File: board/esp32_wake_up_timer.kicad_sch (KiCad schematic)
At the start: 6 parts, among them SW1 SW_DIP_x01, SW3 Rotary Encoder

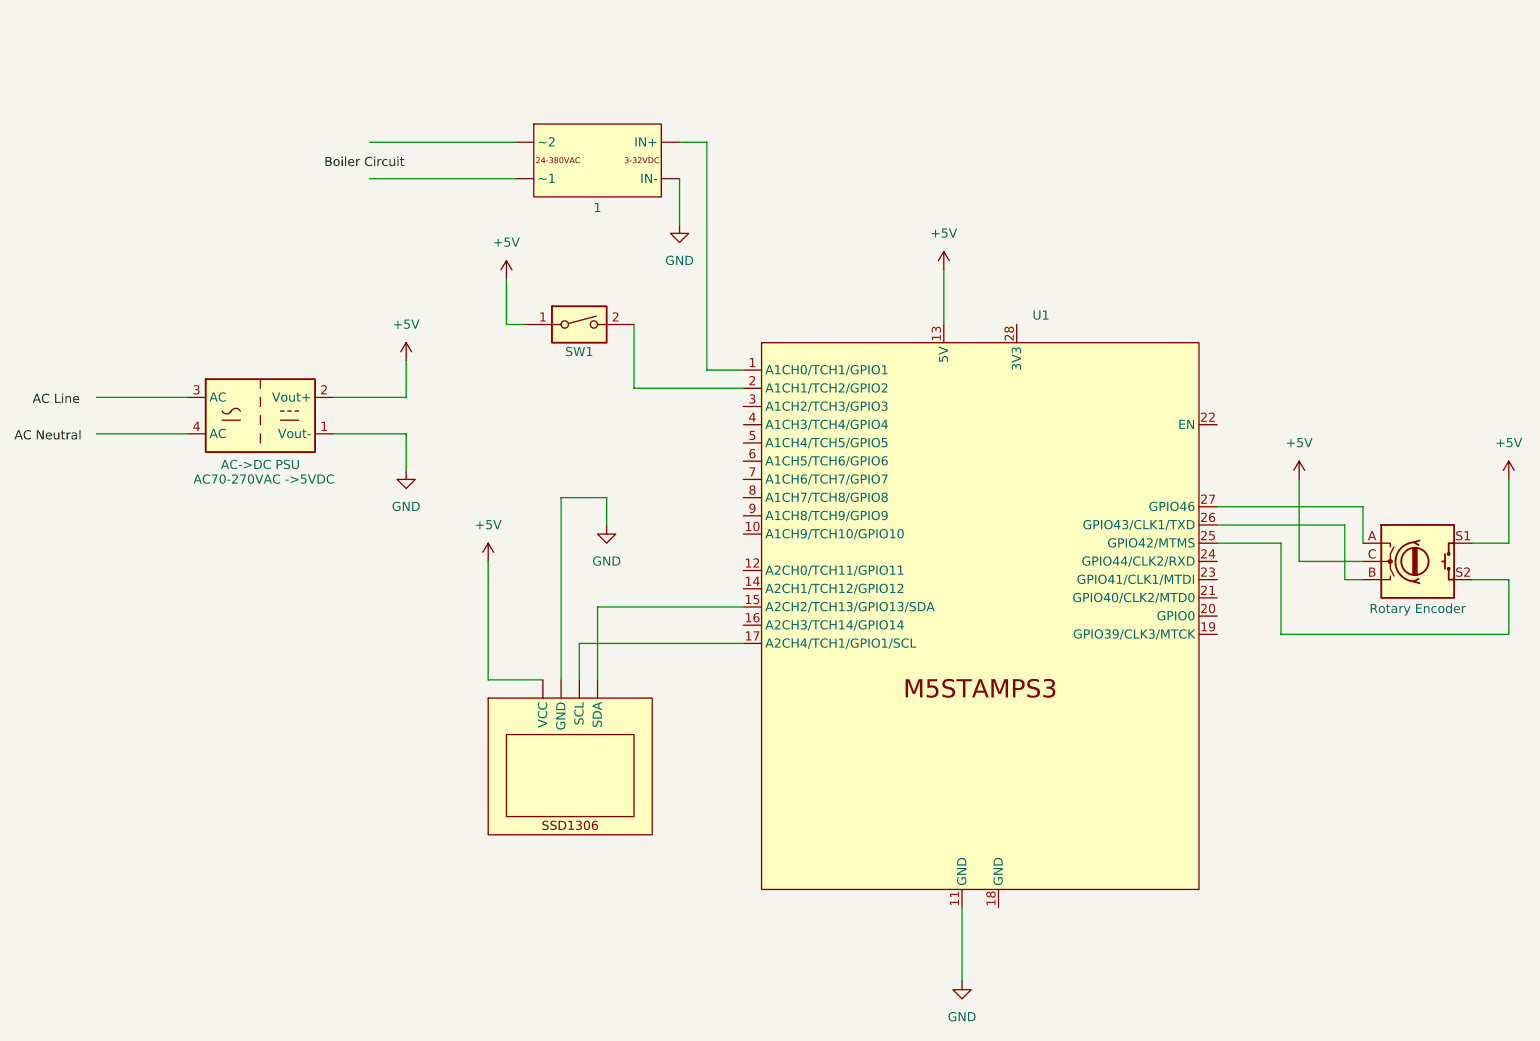
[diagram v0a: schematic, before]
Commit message: Update the schematic to match the pins in the source.
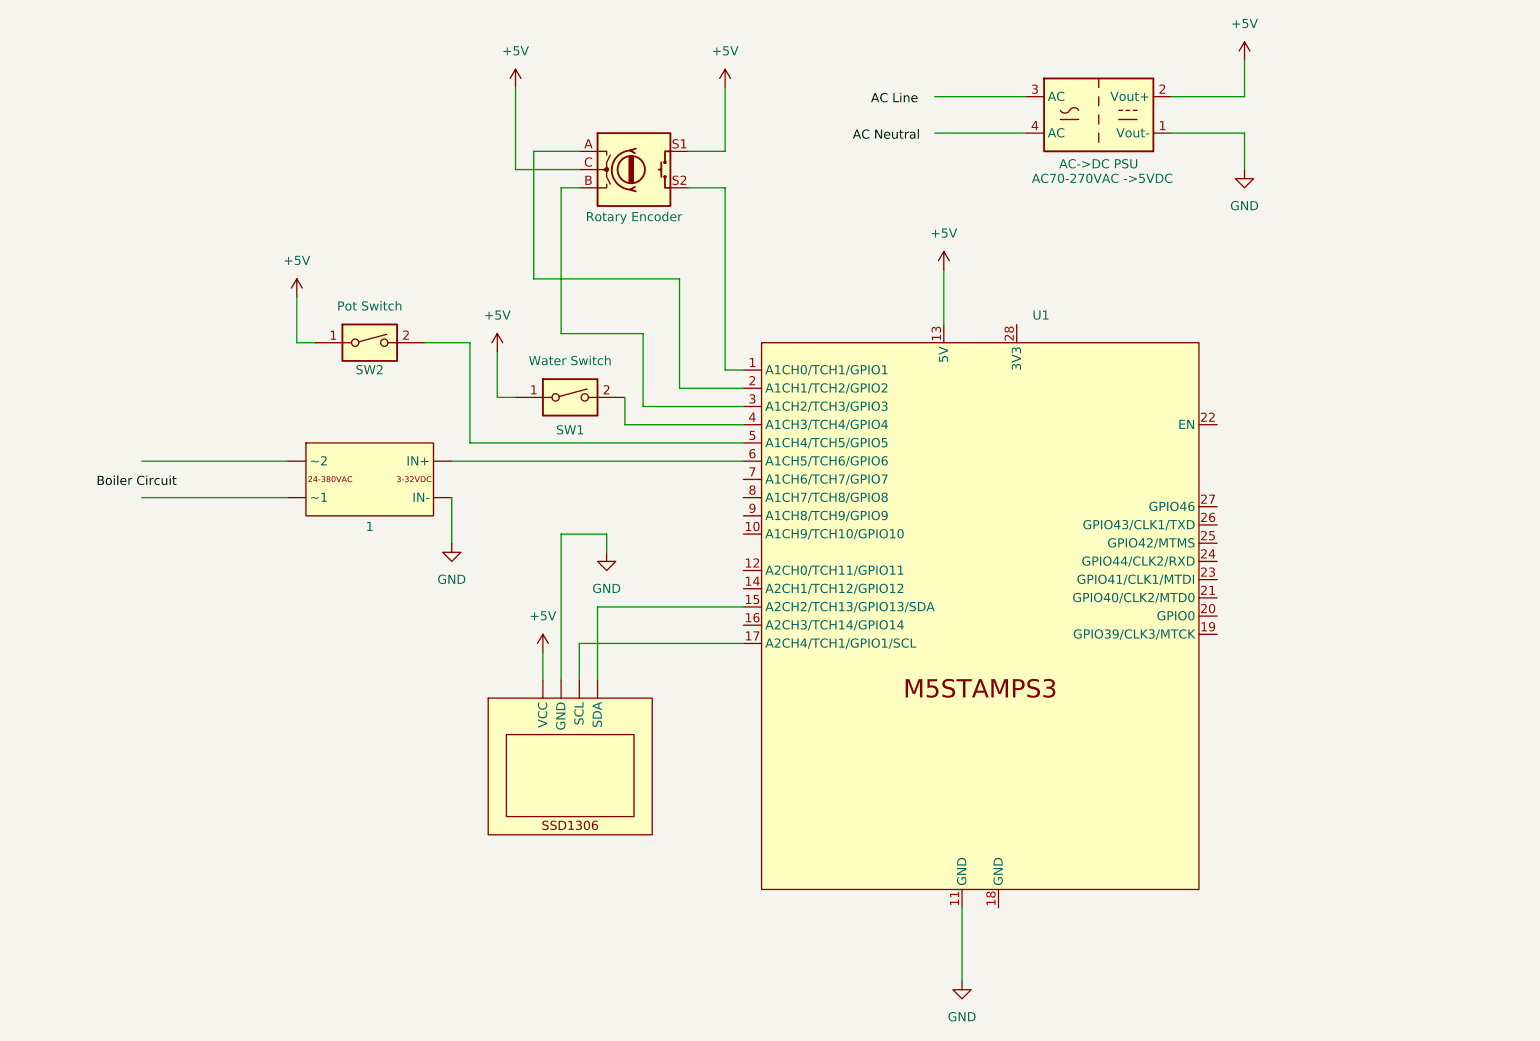
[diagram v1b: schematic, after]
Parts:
- added SW2: Pot Switch, symbol Switch:SW_DIP_x01
- SW1: value SW_DIP_x01 -> Water Switch
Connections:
- net +5V: now also SW2.1
- net at U1.1 (A1CH0/TCH1/GPIO1): now also SW3.S2; no longer 1. (~2)
- net at U1.2 (A1CH1/TCH2/GPIO2): now also SW3.A; no longer SW1.2
- net at U1.25 (GPIO42/MTMS): no longer SW3.S2
- net at U1.26 (GPIO43/CLK1/TXD): no longer SW3.B
- net at U1.27 (GPIO46): no longer SW3.A
- net at U1.3 (A1CH2/TCH3/GPIO3): now also SW3.B
- net at U1.4 (A1CH3/TCH4/GPIO4): now also SW1.2
- net at U1.5 (A1CH4/TCH5/GPIO5): now also SW2.2
- net at U1.6 (A1CH5/TCH6/GPIO6): now also 1. (IN-)
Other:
- moved on the sheet: 1, SW1
